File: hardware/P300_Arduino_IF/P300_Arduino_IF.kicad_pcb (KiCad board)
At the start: 2 copper layers, 29 parts, among them J1 Relay brd, J10 Pressure, J11 TGS2600, J12 I2C (DAC), J13 CO2, J14 5V, J2 DHT1, J3 DHT2, J4 Fan control, J5 TEMP1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

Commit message: Update der Platinen auf 0.23-dev
Änderungen von 0.22 zu 0.23 - P300_Arduino_IF
 - Linke Seite der Platine vergrößert auf ArduinoMega-Größe
 - Stecker für Displayanschluß ergänzt
 - Fünf weitere Bohrungen für Befestigung ergänzt
 - Leiterbahnen im größeren Abstand zu Durchbohrungen und Bauteilen verlegt
 - Connector für J12 I2C nach links verschoben, damit ausreichend Platz für JTS Stecker
 - Auf dem Stecker J4 sind die beiden Lüfteranschlüsse Lüfter 1 und Lüfter 2 getauscht. Damit ist der Stecker kompatibel zu Pluggit. Der Pluggit-Lüfter-Steuerstecker kann direkt aufgesteckt werden, wenn Molex Stiftleiste - KK - 1x8-polig - Stecker, Molex-Best-Nr. 22272081 verwendet wird.

Änderungen von 0.22 zu 0.23 - P300_HiVolt
 - 230V Lüfteranschluss kompatibel zu Pluggit, Molex Stiftleiste - Mini-Fit Jr - 2x4-polig - Stecker, Molex-Best-Nr. 39281083
 - Stecker J3, J4 für Relais auf Molex Stiftleiste - Mini-Fit Jr - 2x3-polig - Stecker, Molex-Best-Nr. 39288060 geändert.
 - Änderung der Belegung der Stecker J3, J4 für die Verwendung es Relaisboards mit den Ralaisanschlüssen: Mitte = Stromzuführung, links = Nicht geschaltet, rechts geschaltet
 - Räumliche Trennung von 230V und Niedervoltspannungen auf der Platine
 
Neu 0.23 - P300_Display_IF
 - Platine zum Aufstecken des Displays für die räumlich getrennte Montage von Display zu P300_Arduino_IF
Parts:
- added ?: MountingHole_3.5mm, Mounting_Holes:MountingHole_3.5mm, F.Cu at (237.5, 119.4)
- added ?: MountingHole_3.5mm, Mounting_Holes:MountingHole_3.5mm, F.Cu at (237.5, 71.1)
- added ?: MountingHole_3.5mm, Mounting_Holes:MountingHole_3.5mm, F.Cu at (142.2, 114.3)
- added ?: MountingHole_3.5mm, Mounting_Holes:MountingHole_3.5mm, F.Cu at (142.2, 86.4)
- added ?: MountingHole_3.5mm, Mounting_Holes:MountingHole_3.5mm, F.Cu at (91.4, 71.1)
- added J15: TFT Display 1, Connectors_Molex:Molex_KK-6410-08_08x2.54mm_Straight, F.Cu at (164.5, 103.5)
- added J16: TFT Display 2, Connectors_Molex:Molex_KK-6410-08_08x2.54mm_Straight, F.Cu at (153.7, 103.5)
- J12: value I2C (DAC) -> I2C
- moved J12 2.54 mm to (191.8, 73.7)
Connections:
- J4 pad 1: Tacho_L1 -> Tacho_L2
- J4 pad 5: Tacho_L2 -> Tacho_L1
- R5 pad 2: PWM_L1 -> PWM_L2
- R6 pad 2: PWM_L2 -> PWM_L1
- XA1 pad 3V3: Net-(XA1-Pad3V3) -> +3V3
- XA1 pad A0: Net-(XA1-PadA0) -> LCD_RD
- XA1 pad A1: Net-(XA1-PadA1) -> LCD_WR
- XA1 pad A2: Net-(XA1-PadA2) -> LCD_RS
- XA1 pad A3: Net-(XA1-PadA3) -> LCD_CS
- XA1 pad A4: Net-(XA1-PadA4) -> LCD_RST
- XA1 pad D10: Net-(XA1-PadD10) -> LCD_D5
- XA1 pad D11: Net-(XA1-PadD11) -> LCD_D4
- XA1 pad D12: Net-(XA1-PadD12) -> LCD_D3
- XA1 pad D13: Net-(XA1-PadD13) -> LCD_D2
- XA1 pad D6: Net-(XA1-PadD6) -> LCD_D1
- XA1 pad D7: Net-(XA1-PadD7) -> LCD_D0
- XA1 pad D8: Net-(XA1-PadD8) -> LCD_D7
- XA1 pad D9: Net-(XA1-PadD9) -> LCD_D6
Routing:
- net +3V3: track 0.00 -> 74.8 mm
- net LCD_D2: track 0.00 -> 69.2 mm
- net LCD_D3: track 0.00 -> 64.5 mm
- net LCD_D4: track 0.00 -> 59.8 mm
- net LCD_D5: track 0.00 -> 55.0 mm
- net LCD_RD: track 0.00 -> 53.2 mm
- net LCD_D6: track 0.00 -> 50.3 mm
- net LCD_WR: track 0.00 -> 49.5 mm
- net LCD_RS: track 0.00 -> 45.9 mm
- net LCD_D7: track 0.00 -> 45.6 mm
- net LCD_CS: track 0.00 -> 42.5 mm
- net LCD_D0: track 0.00 -> 42.4 mm
- net LCD_RST: track 0.00 -> 39.1 mm
- net LCD_D1: track 0.00 -> 36.0 mm
- net +5V: track 208.6 -> 240.2 mm
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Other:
- board text added: "Arduino-Ctrl Pluggit P300/P450 Rev 0.23-dev"
- board text added: "GND"
- board text removed: "Arduino-Ctrl Pluggit P300/P450 Rev 0.22-dev"

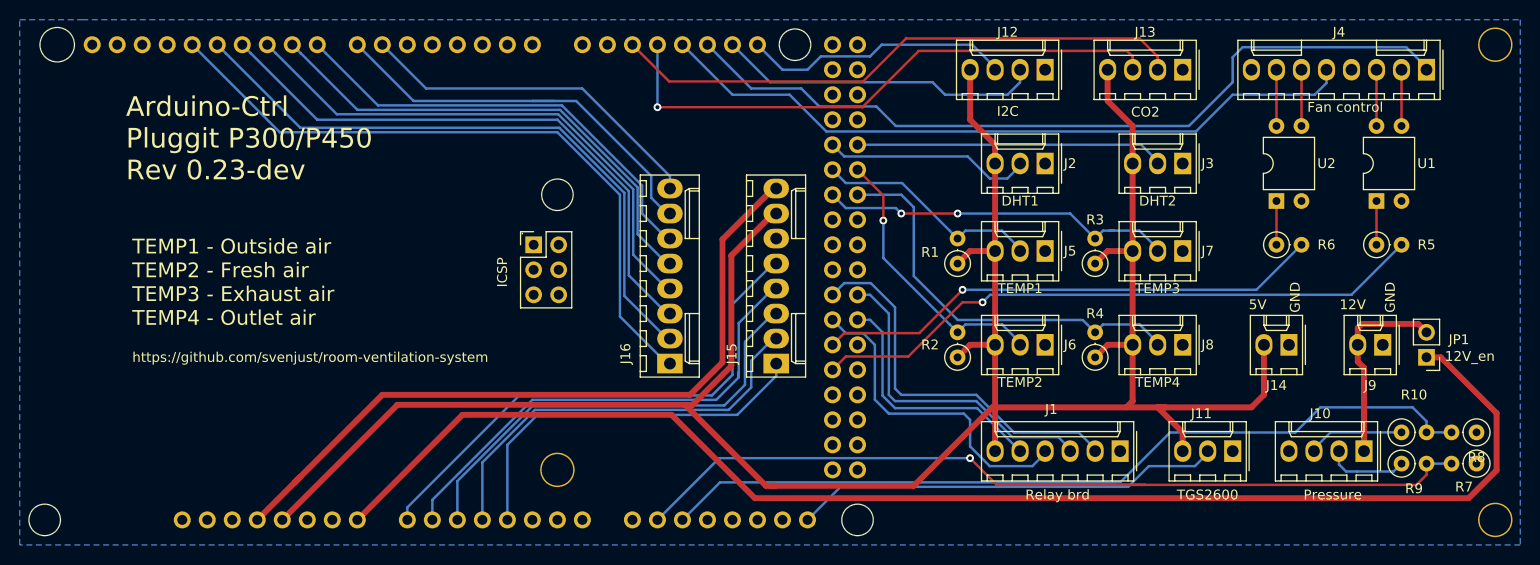
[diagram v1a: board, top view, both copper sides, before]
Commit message: Masseverbindungen auf J4 ergänzt.
Auf dem Stecker J4 (Lüfteranschluss) die vergessenen Masseverbindungen Pin 4 und Pin 8 ergänzt.
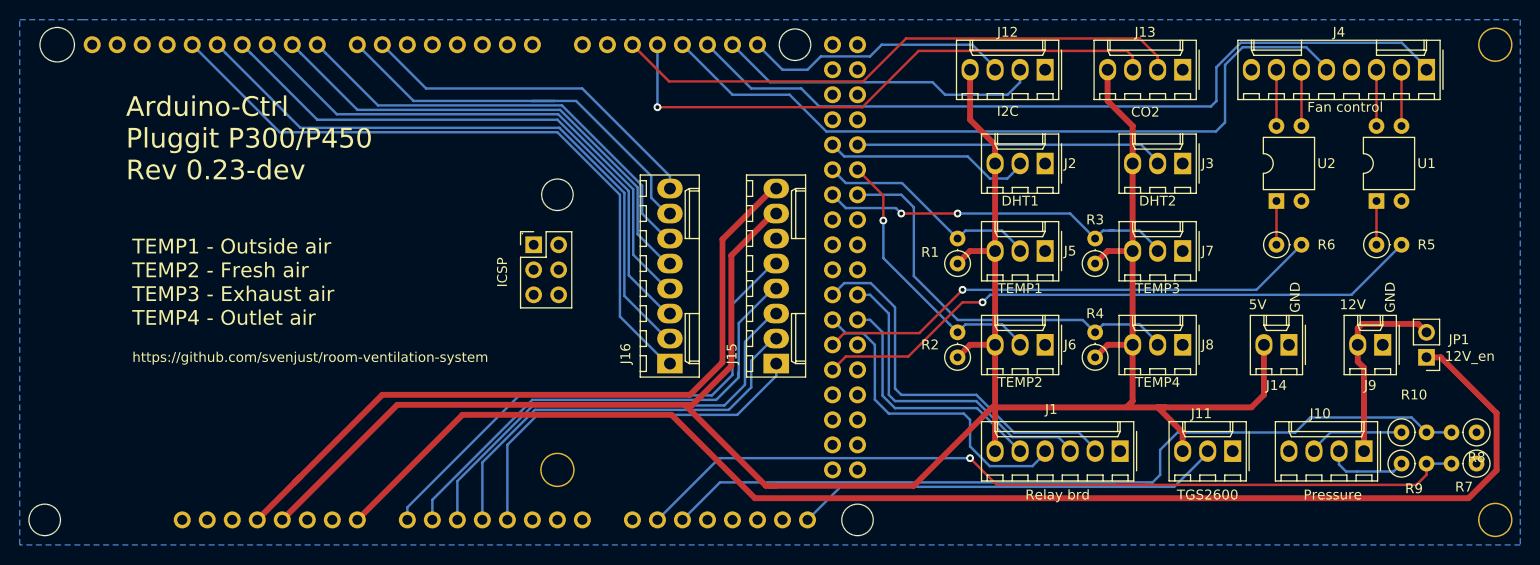
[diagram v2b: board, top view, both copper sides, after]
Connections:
- J4 pad 4: Net-(J4-Pad4) -> GND
- J4 pad 8: Net-(J4-Pad8) -> GND
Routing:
- net Tacho_L1: track 72.4 -> 77.1 mm
- net Tacho_L2: track 82.3 -> 81.6 mm

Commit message: Platinen V.23 in die Herstellung gegeben
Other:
- board text added: "Arduino-Ctrl Pluggit P300/P450 Rev 0.23"
- board text removed: "Arduino-Ctrl Pluggit P300/P450 Rev 0.23-dev"
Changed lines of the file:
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@@
     (add_net "Net-(JP1-Pad1)")
+  )
+  (module Resistors_THT:R_Axial_DIN0207_L6.3mm_D2.5mm_P2.54mm_Vertical (layer F.Cu)
+    (at 182.88 93.345 90)
+    (descr "Resistor, Axial_DIN0207 series, Axial, Vertical, pin pitch=2.54mm, 0.25W = 1/4W, length*diameter=6.3*2.5mm^2, http://cdn-reichelt.de/documents/datenblatt/B400/1_4W%23YAG.pdf")
+    (tags "Resistor Axial_DIN0207 series Axial Vertical pin pitch 2.54mm 0.25W = 1/4W length 6.3mm diameter 2.5mm")
+    (fp_text reference R1 (at 1.143 -2.794 180) (layer F.SilkS)
+      (effects (font (size 1 1) (thickness 0.15)))
+    )
+    (fp_text value 4.7k (at 1.27 2.31 90) (layer F.Fab)
+      (effects (font (size 1 1) (thickness 0.15)))
+    )
+    (fp_circle (center 0 0) (end 1.25 0) (layer F.Fab) (width 0.1))
+    (fp_circle (center 0 0) (end 1.31 0) (layer F.SilkS) (width 0.12))
+    (fp_line (start 0 0) (end 2.54 0) (layer F.Fab) (width 0.1))
+    (fp_line (start 1.31 0) (end 1.44 0) (layer F.SilkS) (width 0.12))
+    (fp_line (start -1.6 -1.6) (end -1.6 1.6) (layer F.CrtYd) (width 0.05))
+    (fp_line (start -1.6 1.6) (end 3.65 1.6) (layer F.CrtYd) (width 0.05))
+    (fp_line (start 3.65 1.6) (end 3.65 -1.6) (layer F.CrtYd) (width 0.05))
+    (fp_line (start 3.65 -1.6) (end -1.6 -1.6) (layer F.CrtYd) (width 0.05))
+    (pad 1 thru_hole circle (at 0 0 90) (size 1.6 1.6) (drill 0.8) (layers *.Cu *.Mask)
+      (net 29 +5V))
+    (pad 2 thru_hole oval (at 2.54 0 90) (size 1.6 1.6) (drill 0.8) (layers *.Cu *.Mask)
+      (net 49 TEMP1))
+    (model ${KISYS3DMOD}/Resistors_THT.3dshapes/R_Axial_DIN0207_L6.3mm_D2.5mm_P2.54mm_Vertical.wrl
+      (at (xyz 0 0 0))
+      (scale (xyz 0.393701 0.393701 0.393701))
+      (rotate (xyz 0 0 0))
+    )
   )
   (module Arduino:Arduino_Mega2560_Shield_no_ICSP (layer F.Cu)
@@
   )
   (module Resistors_THT:R_Axial_DIN0207_L6.3mm_D2.5mm_P2.54mm_Vertical (layer F.Cu)
-    (at 182.88 93.345 90)
-    (descr "Resistor, Axial_DIN0207 series, Axial, Vertical, pin pitch=2.54mm, 0.25W = 1/4W, length*diameter=6.3*2.5mm^2, http://cdn-reichelt.de/documents/datenblatt/B400/1_4W%23YAG.pdf")
-    (tags "Resistor Axial_DIN0207 series Axial Vertical pin pitch 2.54mm 0.25W = 1/4W length 6.3mm diameter 2.5mm")
-    (fp_text reference R1 (at 1.143 -2.794 180) (layer F.SilkS)
-      (effects (font (size 1 1) (thickness 0.15)))
-    )
-    (fp_text value 4.7k (at 1.27 2.31 90) (layer F.Fab)
-      (effects (font (size 1 1) (thickness 0.15)))
-    )
-    (fp_circle (center 0 0) (end 1.25 0) (layer F.Fab) (width 0.1))
-    (fp_circle (center 0 0) (end 1.31 0) (layer F.SilkS) (width 0.12))
-    (fp_line (start 0 0) (end 2.54 0) (layer F.Fab) (width 0.1))
-    (fp_line (start 1.31 0) (end 1.44 0) (layer F.SilkS) (width 0.12))
-    (fp_line (start -1.6 -1.6) (end -1.6 1.6) (layer F.CrtYd) (width 0.05))
-    (fp_line (start -1.6 1.6) (end 3.65 1.6) (layer F.CrtYd) (width 0.05))
-    (fp_line (start 3.65 1.6) (end 3.65 -1.6) (layer F.CrtYd) (width 0.05))
-    (fp_line (start 3.65 -1.6) (end -1.6 -1.6) (layer F.CrtYd) (width 0.05))
-    (pad 1 thru_hole circle (at 0 0 90) (size 1.6 1.6) (drill 0.8) (layers *.Cu *.Mask)
-      (net 29 +5V))
-    (pad 2 thru_hole oval (at 2.54 0 90) (size 1.6 1.6) (drill 0.8) (layers *.Cu *.Mask)
-      (net 49 TEMP1))
-    (model ${KISYS3DMOD}/Resistors_THT.3dshapes/R_Axial_DIN0207_L6.3mm_D2.5mm_P2.54mm_Vertical.wrl
-      (at (xyz 0 0 0))
-      (scale (xyz 0.393701 0.393701 0.393701))
-      (rotate (xyz 0 0 0))
-    )
-  )
-  (module Resistors_THT:R_Axial_DIN0207_L6.3mm_D2.5mm_P2.54mm_Vertical (layer F.Cu)
     (at 215.265 91.44)
     (descr "Resistor, Axial_DIN0207 series, Axial, Vertical, pin pitch=2.54mm, 0.25W = 1/4W, length*diameter=6.3*2.5mm^2, http://cdn-reichelt.de/documents/datenblatt/B400/1_4W%23YAG.pdf")
@@
     (effects (font (size 1.5 1.5) (thickness 0.3)) (justify left))
   )
-  (gr_text "Arduino-Ctrl\nPluggit P300/P450\nRev 0.23-dev" (at 98.425 80.645) (layer F.SilkS)
+  (gr_text "Arduino-Ctrl\nPluggit P300/P450\nRev 0.23" (at 98.425 80.645) (layer F.SilkS)
     (effects (font (size 2 2) (thickness 0.3)) (justify left))
   )
